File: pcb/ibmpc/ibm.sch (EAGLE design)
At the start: 31 parts, among them J2 ATX24RH

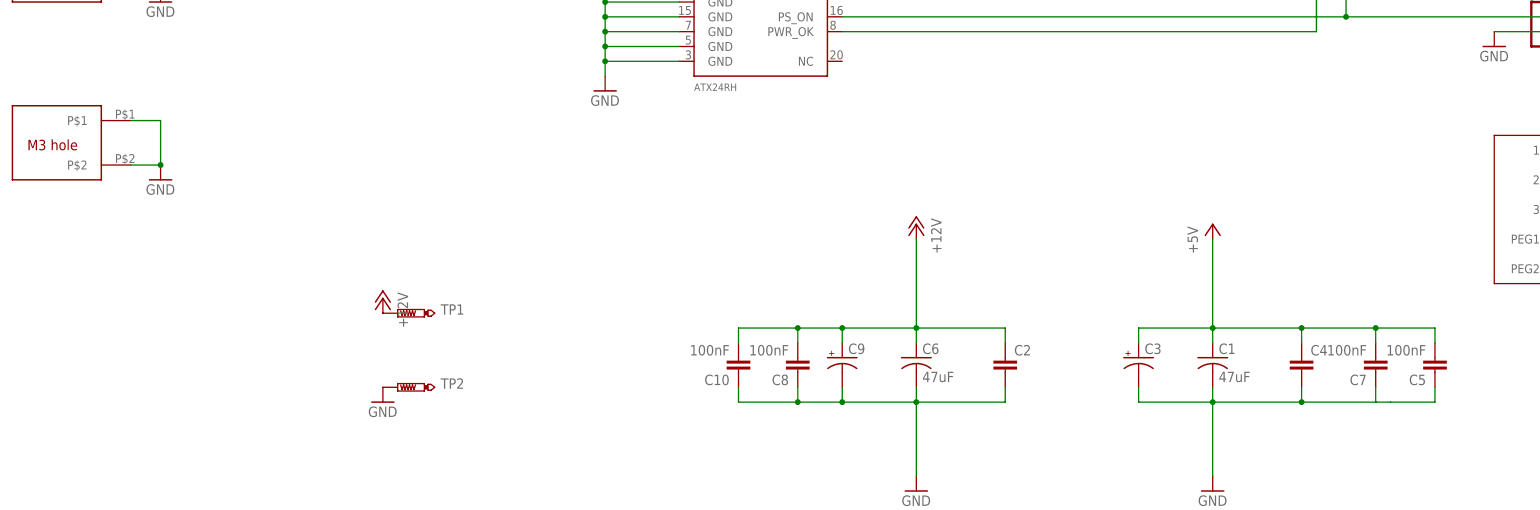
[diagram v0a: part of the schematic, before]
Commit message: changed to small diameter caps
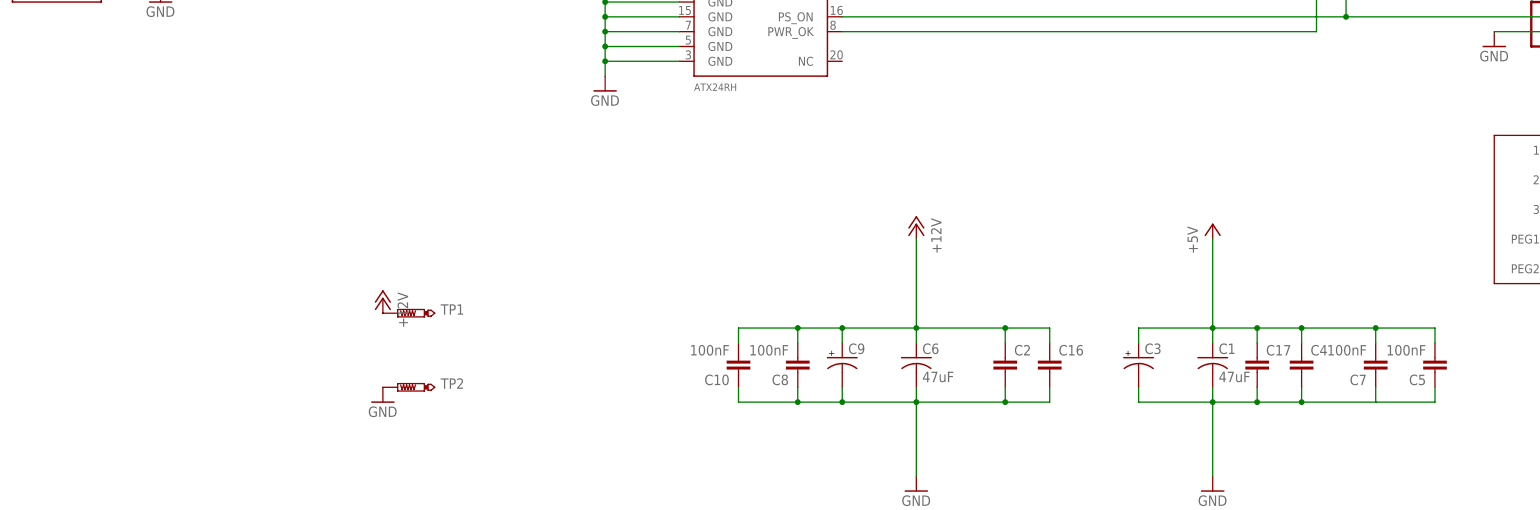
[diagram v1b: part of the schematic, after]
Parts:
- removed U$7: M3_MOUNTING_HOLE, apricot:M3_MOUNTING_HOLE
- added C16, C17: (no value), capacitor-wima:C5/2.5
- C12, C3, C9: device adafruit:CPOL-USE5-10.5 -> adafruit_changed:CPOL-USE3.5-8
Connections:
- net +12V: now also C16.1
- net +5V: now also C17.1
- net GND: now also C16.2, C17.2; no longer U$7.P$1, U$7.P$2
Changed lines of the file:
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@@
 <part name="U$3" library="atx_power_control" deviceset="CAR_FUSE_HOLDER" device="3IN1"/>
 <part name="+3V1" library="supply1" library_urn="urn:adsk.eagle:library:371" deviceset="+3V3" device=""/>
-<part name="C9" library="adafruit" deviceset="CPOL-US" device="E5-10.5"/>
+<part name="C9" library="adafruit_changed" deviceset="CPOL-US" device="E3.5-8"/>
 <part name="C2" library="capacitor-wima" library_urn="urn:adsk.eagle:library:116" deviceset="C" device="5/2.5" package3d_urn="urn:adsk.eagle:package:5426/1"/>
 <part name="C1" library="clock" deviceset="C-US" device="C1210" value="47uF"/>
 <part name="GND1" library="supply1" library_urn="urn:adsk.eagle:library:371" deviceset="GND" device=""/>
-<part name="C3" library="adafruit" deviceset="CPOL-US" device="E5-10.5"/>
+<part name="C3" library="adafruit_changed" deviceset="CPOL-US" device="E3.5-8"/>
 <part name="C4" library="capacitor-wima" library_urn="urn:adsk.eagle:library:116" deviceset="C" device="5/2.5" package3d_urn="urn:adsk.eagle:package:5426/1"/>
 <part name="P+1" library="supply1" library_urn="urn:adsk.eagle:library:371" deviceset="+5V" device=""/>
@@
 <part name="C11" library="clock" deviceset="C-US" device="C1210" value="47uF"/>
 <part name="GND3" library="supply1" library_urn="urn:adsk.eagle:library:371" deviceset="GND" device=""/>
-<part name="C12" library="adafruit" deviceset="CPOL-US" device="E5-10.5"/>
+<part name="C12" library="adafruit_changed" deviceset="CPOL-US" device="E3.5-8"/>
 <part name="+3V2" library="supply1" library_urn="urn:adsk.eagle:library:371" deviceset="+3V3" device=""/>
 <part name="GND5" library="supply1" library_urn="urn:adsk.eagle:library:371" deviceset="GND" device=""/>
@@
 <part name="GND13" library="supply1" library_urn="urn:adsk.eagle:library:371" deviceset="GND" device=""/>
 <part name="P+5" library="supply1" library_urn="urn:adsk.eagle:library:371" deviceset="+12V" device=""/>
-<part name="U$7" library="apricot" deviceset="M3_MOUNTING_HOLE" device=""/>
-<part name="GND14" library="supply1" library_urn="urn:adsk.eagle:library:371" deviceset="GND" device=""/>
 <part name="IC1" library="v-reg" library_urn="urn:adsk.eagle:library:409" deviceset="79XXS" device="" package3d_urn="urn:adsk.eagle:package:30343/1"/>
+<part name="C16" library="capacitor-wima" library_urn="urn:adsk.eagle:library:116" deviceset="C" device="5/2.5" package3d_urn="urn:adsk.eagle:package:5426/1"/>
+<part name="C17" library="capacitor-wima" library_urn="urn:adsk.eagle:library:116" deviceset="C" device="5/2.5" package3d_urn="urn:adsk.eagle:package:5426/1"/>
 </parts>
 <sheets>
@@
 <attribute name="VALUE" x="33.02" y="109.22" size="1.778" layer="96" rot="MR90"/>
 </instance>
-<instance part="U$7" gate="G$1" x="-35.56" y="139.7" smashed="yes"/>
-<instance part="GND14" gate="1" x="-7.62" y="134.62" smashed="yes">
-<attribute name="VALUE" x="-10.16" y="132.08" size="1.778" layer="96"/>
-</instance>
 <instance part="IC1" gate="1" x="177.8" y="231.14" smashed="yes">
 <attribute name="NAME" x="180.34" y="240.03" size="1.778" layer="95"/>
 <attribute name="VALUE" x="180.34" y="237.49" size="1.778" layer="96"/>
+</instance>
+<instance part="C16" gate="G$1" x="144.78" y="104.14" smashed="yes">
+<attribute name="NAME" x="146.304" y="104.521" size="1.778" layer="95"/>
+<attribute name="VALUE" x="146.304" y="99.441" size="1.778" layer="96"/>
+</instance>
+<instance part="C17" gate="G$1" x="180.34" y="104.14" smashed="yes">
+<attribute name="NAME" x="181.864" y="104.521" size="1.778" layer="95"/>
+<attribute name="VALUE" x="181.864" y="99.441" size="1.778" layer="96"/>
 </instance>
 </instances>
@@
 <wire x1="101.6" y1="99.06" x2="101.6" y2="96.52" width="0.1524" layer="91"/>
 <junction x="101.6" y="96.52"/>
+<pinref part="C16" gate="G$1" pin="2"/>
+<wire x1="137.16" y1="96.52" x2="144.78" y2="96.52" width="0.1524" layer="91"/>
+<wire x1="144.78" y1="96.52" x2="144.78" y2="99.06" width="0.1524" layer="91"/>
+<junction x="137.16" y="96.52"/>
 </segment>
 <segment>
@@
 <junction x="172.72" y="96.52"/>
 <pinref part="C4" gate="G$1" pin="2"/>
-<wire x1="172.72" y1="96.52" x2="187.96" y2="96.52" width="0.1524" layer="91"/>
+<wire x1="172.72" y1="96.52" x2="180.34" y2="96.52" width="0.1524" layer="91"/>
+<wire x1="180.34" y1="96.52" x2="187.96" y2="96.52" width="0.1524" layer="91"/>
 <wire x1="187.96" y1="96.52" x2="187.96" y2="99.06" width="0.1524" layer="91"/>
 <pinref part="C5" gate="G$1" pin="1"/>
 <wire x1="210.82" y1="99.06" x2="210.82" y2="96.52" width="0.1524" layer="91"/>
-<wire x1="210.82" y1="96.52" x2="203.2" y2="96.52" width="0.1524" layer="91"/>
+<wire x1="210.82" y1="96.52" x2="200.66" y2="96.52" width="0.1524" layer="91"/>
 <junction x="187.96" y="96.52"/>
 <pinref part="C7" gate="G$1" pin="1"/>
 <wire x1="200.66" y1="96.52" x2="187.96" y2="96.52" width="0.1524" layer="91"/>
 <wire x1="200.66" y1="99.06" x2="200.66" y2="96.52" width="0.1524" layer="91"/>
-<wire x1="200.66" y1="96.52" x2="203.2" y2="96.52" width="0.1524" layer="91"/>
+<pinref part="C17" gate="G$1" pin="2"/>
+<wire x1="180.34" y1="99.06" x2="180.34" y2="96.52" width="0.1524" layer="91"/>
+<junction x="180.34" y="96.52"/>
 </segment>
 <segment>
@@
 <pinref part="TP2" gate="G$1" pin="TP"/>
 <pinref part="GND13" gate="1" pin="GND"/>
-</segment>
-<segment>
-<pinref part="GND14" gate="1" pin="GND"/>
-<wire x1="-7.62" y1="144.78" x2="-7.62" y2="137.16" width="0.1524" layer="91"/>
-<pinref part="U$7" gate="G$1" pin="P$1"/>
-<wire x1="-12.7" y1="144.78" x2="-7.62" y2="144.78" width="0.1524" layer="91"/>
-<pinref part="U$7" gate="G$1" pin="P$2"/>
-<wire x1="-12.7" y1="137.16" x2="-7.62" y2="137.16" width="0.1524" layer="91"/>
-<junction x="-7.62" y="137.16"/>
 </segment>
 <segment>
@@
 <junction x="172.72" y="109.22"/>
 <pinref part="C4" gate="G$1" pin="1"/>
-<wire x1="172.72" y1="109.22" x2="187.96" y2="109.22" width="0.1524" layer="91"/>
+<wire x1="172.72" y1="109.22" x2="180.34" y2="109.22" width="0.1524" layer="91"/>
+<wire x1="180.34" y1="109.22" x2="187.96" y2="109.22" width="0.1524" layer="91"/>
 <wire x1="187.96" y1="109.22" x2="187.96" y2="106.68" width="0.1524" layer="91"/>
 <pinref part="P+1" gate="1" pin="+5V"/>
@@
 <wire x1="210.82" y1="109.22" x2="210.82" y2="106.68" width="0.1524" layer="91"/>
 <junction x="200.66" y="109.22"/>
+<pinref part="C17" gate="G$1" pin="1"/>
+<wire x1="180.34" y1="106.68" x2="180.34" y2="109.22" width="0.1524" layer="91"/>
+<junction x="180.34" y="109.22"/>
 </segment>
 <segment>
@@
 <wire x1="101.6" y1="106.68" x2="101.6" y2="109.22" width="0.1524" layer="91"/>
 <junction x="101.6" y="109.22"/>
-</segment>
-<segment>
+<pinref part="C16" gate="G$1" pin="1"/>
+<wire x1="137.16" y1="109.22" x2="144.78" y2="109.22" width="0.1524" layer="91"/>
+<wire x1="144.78" y1="109.22" x2="144.78" y2="106.68" width="0.1524" layer="91"/>
+<junction x="137.16" y="109.22"/>
+</segment>
+<segment>

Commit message: adding fingers
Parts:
- removed C12: (no value), adafruit_changed:CPOL-USE3.5-8
- removed C13, C15: 100nF, clock:CAP0805
- removed U$3: CAR_FUSE_HOLDER3IN1, atx_power_control:CAR_FUSE_HOLDER3IN1
- added IC2: 7805T, linear:7805T
- added U$10, U$7, U$9: ISA, blade:ISA
- C11: value 47uF -> (none); device clock:C-USC1210 -> capacitor-wima:C5/2.5
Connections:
- removed net +3V3: C11.1, C12.+, C13.2, C15.2, U$1.3V3, U$3.B0, U$3.B1
- removed net N$1: J2.3.3V@0, J2.3.3V@1, J2.3.3V@2, J2.3.3V@3, U$3.A0, U$3.A1
- removed net N$2: IC1.IN, J2.-12V, U$1.-12V
- removed net N$7: C14.1, IC1.OUT, U$1.-5V
- new net -12V: C11.1, IC1.IN, J2.-12V, U$1.-12V, U$10.P$1
- new net -5V: C14.1, IC1.OUT, U$1.-5V, U$7.P$1
- net GND: now also U$9.P$1; no longer C12.-, C13.1, C15.1

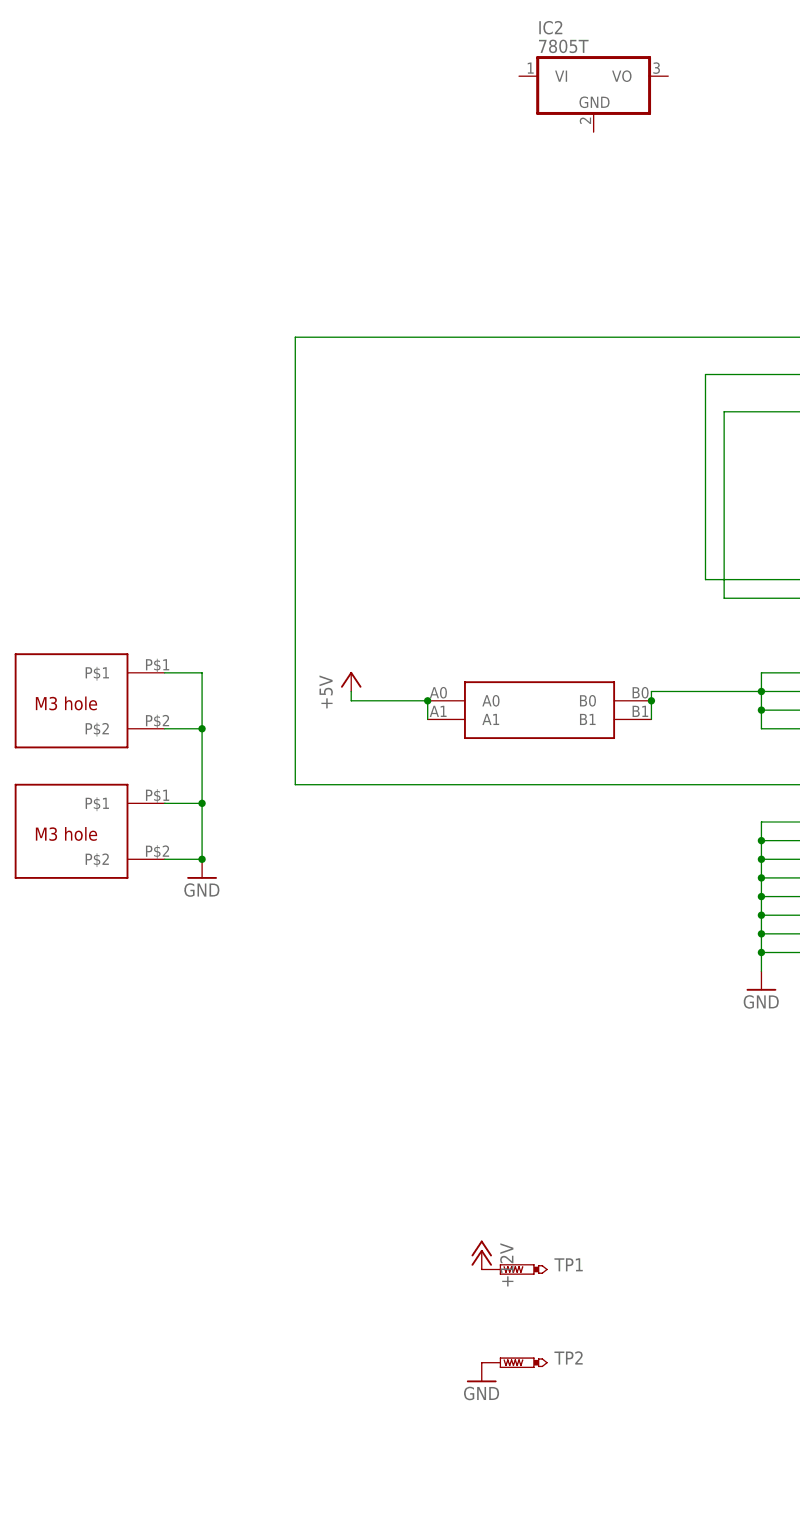
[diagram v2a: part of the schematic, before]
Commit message: added voltage blaster features, removed 3.3V
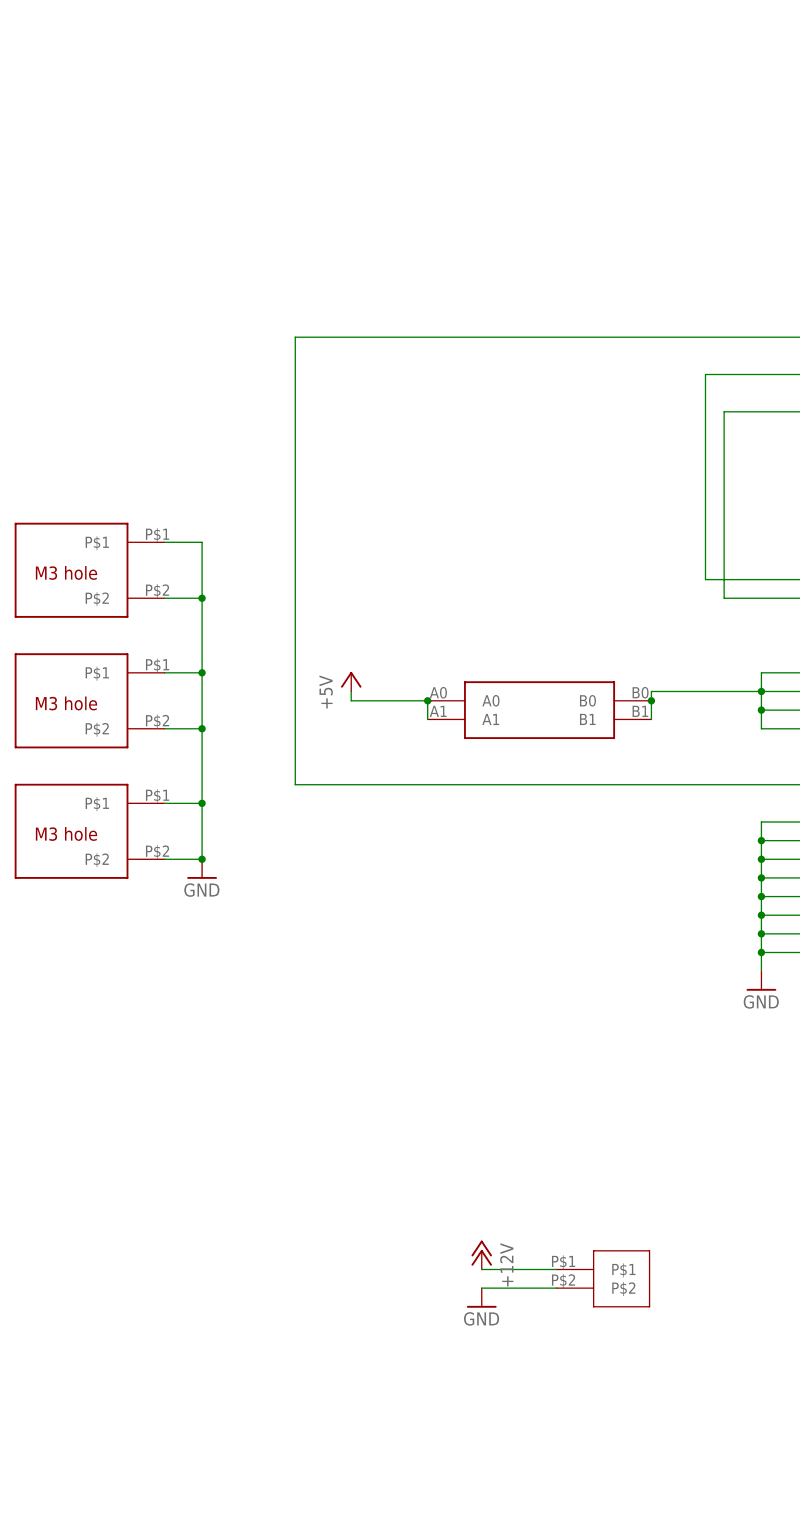
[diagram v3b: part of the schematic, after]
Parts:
- removed IC2: 7805T, linear:7805T
- removed TP1, TP2: PTR1PAD1-20, testpad:PTR1PAD1-20
- added U$11: M3_MOUNTING_HOLE, apricot:M3_MOUNTING_HOLE
- added U$3: VH396_2P, 396_conn:VH396_2P
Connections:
- net +12V: now also U$3.P$1; no longer TP1.TP
- net GND: now also U$11.P$1, U$11.P$2, U$3.P$2; no longer TP2.TP
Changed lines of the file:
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@@
 <part name="R1" library="adafruit" deviceset="R-US_" device="0207/10" value="470"/>
 <part name="GND12" library="supply1" library_urn="urn:adsk.eagle:library:371" deviceset="GND" device=""/>
-<part name="TP1" library="testpad" library_urn="urn:adsk.eagle:library:385" deviceset="PTR1" device="PAD1-20" package3d_urn="urn:adsk.eagle:package:27950/1"/>
-<part name="TP2" library="testpad" library_urn="urn:adsk.eagle:library:385" deviceset="PTR1" device="PAD1-20" package3d_urn="urn:adsk.eagle:package:27950/1"/>
 <part name="GND13" library="supply1" library_urn="urn:adsk.eagle:library:371" deviceset="GND" device=""/>
 <part name="P+5" library="supply1" library_urn="urn:adsk.eagle:library:371" deviceset="+12V" device=""/>
@@
 <part name="GND14" library="supply1" library_urn="urn:adsk.eagle:library:371" deviceset="GND" device=""/>
 <part name="U$10" library="blade" deviceset="ISA" device=""/>
-<part name="IC2" library="linear" library_urn="urn:adsk.eagle:library:262" deviceset="78*" device="T" package3d_urn="urn:adsk.eagle:package:16414/1" technology="05"/>
 <part name="C11" library="capacitor-wima" library_urn="urn:adsk.eagle:library:116" deviceset="C" device="5/2.5" package3d_urn="urn:adsk.eagle:package:5426/1"/>
 <part name="GND3" library="supply1" library_urn="urn:adsk.eagle:library:371" deviceset="GND" device=""/>
 <part name="P-1" library="supply1" library_urn="urn:adsk.eagle:library:371" deviceset="-12V" device=""/>
 <part name="P-2" library="supply1" library_urn="urn:adsk.eagle:library:371" deviceset="-5V" device=""/>
+<part name="U$3" library="396_conn" deviceset="VH396_2P" device=""/>
+<part name="U$11" library="apricot" deviceset="M3_MOUNTING_HOLE" device=""/>
 </parts>
 <sheets>
@@
 <attribute name="VALUE" x="284.48" y="185.42" size="1.778" layer="96"/>
 </instance>
-<instance part="TP1" gate="G$1" x="33.02" y="111.76" smashed="yes" rot="R90">
-<attribute name="NAME" x="44.45" y="113.284" size="1.778" layer="95" rot="R180"/>
-<attribute name="TP_SIGNAL_NAME" x="35.56" y="113.03" size="1.778" layer="97" rot="R90"/>
-</instance>
-<instance part="TP2" gate="G$1" x="33.02" y="99.06" smashed="yes" rot="R90">
-<attribute name="NAME" x="44.45" y="100.584" size="1.778" layer="95" rot="R180"/>
-<attribute name="TP_SIGNAL_NAME" x="35.56" y="100.33" size="1.778" layer="97" rot="R90"/>
-</instance>
-<instance part="GND13" gate="1" x="30.48" y="96.52" smashed="yes">
-<attribute name="VALUE" x="27.94" y="93.98" size="1.778" layer="96"/>
+<instance part="GND13" gate="1" x="30.48" y="106.68" smashed="yes">
+<attribute name="VALUE" x="27.94" y="104.14" size="1.778" layer="96"/>
 </instance>
 <instance part="P+5" gate="1" x="30.48" y="114.3" smashed="yes" rot="MR0">
@@
 </instance>
 <instance part="U$10" gate="G$1" x="228.6" y="248.92" smashed="yes" rot="R180"/>
-<instance part="IC2" gate="A1" x="45.72" y="274.32" smashed="yes">
-<attribute name="NAME" x="38.1" y="280.035" size="1.778" layer="95"/>
-<attribute name="VALUE" x="38.1" y="277.495" size="1.778" layer="96"/>
-</instance>
 <instance part="C11" gate="G$1" x="154.94" y="246.38" smashed="yes">
 <attribute name="NAME" x="156.464" y="246.761" size="1.778" layer="95"/>
@@
 <attribute name="VALUE" x="190.5" y="218.44" size="1.778" layer="96" rot="R90"/>
 </instance>
+<instance part="U$3" gate="G$1" x="45.72" y="111.76" smashed="yes"/>
+<instance part="U$11" gate="G$1" x="-35.56" y="205.74" smashed="yes"/>
 </instances>
 <busses>
@@
 <wire x1="-12.7" y1="167.64" x2="-7.62" y2="167.64" width="0.1524" layer="91"/>
 <junction x="-7.62" y="167.64"/>
+<pinref part="U$11" gate="G$1" pin="P$1"/>
+<wire x1="-12.7" y1="210.82" x2="-7.62" y2="210.82" width="0.1524" layer="91"/>
+<wire x1="-7.62" y1="210.82" x2="-7.62" y2="203.2" width="0.1524" layer="91"/>
+<junction x="-7.62" y="193.04"/>
+<pinref part="U$11" gate="G$1" pin="P$2"/>
+<wire x1="-7.62" y1="203.2" x2="-7.62" y2="193.04" width="0.1524" layer="91"/>
+<wire x1="-12.7" y1="203.2" x2="-7.62" y2="203.2" width="0.1524" layer="91"/>
+<junction x="-7.62" y="203.2"/>
 </segment>
 <segment>
@@
 </segment>
 <segment>
-<pinref part="TP2" gate="G$1" pin="TP"/>
-<pinref part="GND13" gate="1" pin="GND"/>
-</segment>
-<segment>
 <pinref part="GND7" gate="1" pin="GND"/>
 <wire x1="177.8" y1="241.3" x2="177.8" y2="238.76" width="0.1524" layer="91"/>
@@
 <pinref part="C11" gate="G$1" pin="2"/>
 <pinref part="GND3" gate="1" pin="GND"/>
+</segment>
+<segment>
+<pinref part="GND13" gate="1" pin="GND"/>
+<pinref part="U$3" gate="G$1" pin="P$2"/>
+<wire x1="30.48" y1="109.22" x2="40.64" y2="109.22" width="0.1524" layer="91"/>
 </segment>
 </net>
@@
 </segment>
 <segment>
-<pinref part="TP1" gate="G$1" pin="TP"/>
 <pinref part="P+5" gate="1" pin="+12V"/>
+<pinref part="U$3" gate="G$1" pin="P$1"/>
+<wire x1="30.48" y1="111.76" x2="40.64" y2="111.76" width="0.1524" layer="91"/>
 </segment>
 </net>
